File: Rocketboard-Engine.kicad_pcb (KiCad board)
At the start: 2 copper layers, 26 x 53.1 mm, 31 parts, among them IC1 STM32L072CBT6, J1 SWD Port, J2 USB_C_Receptacle_USB2.0, J3 Conn_01x20, J4 Conn_01x20, Q1 BSS138, U1 USBLC6-2SC6, U2 AMS1117-3.3

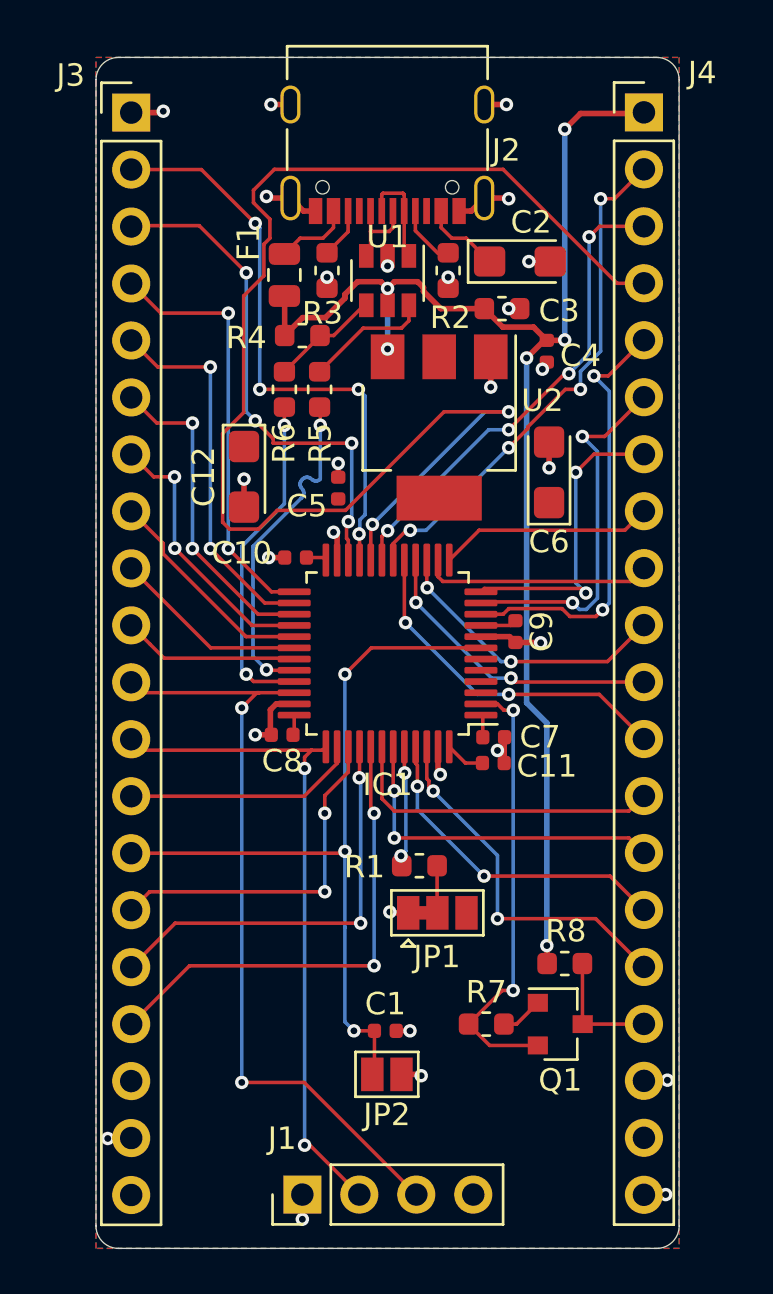
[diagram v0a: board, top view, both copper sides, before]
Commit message: Fixed unconnected copper pours/nets
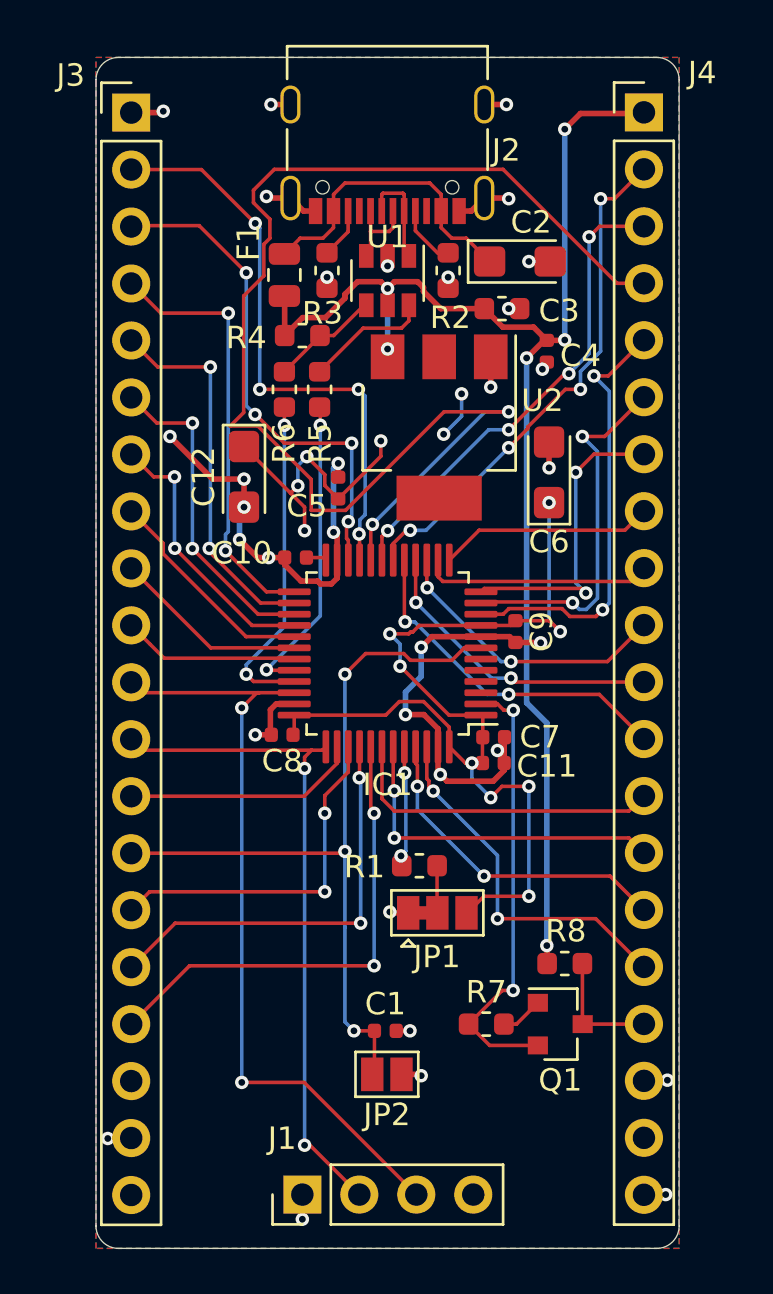
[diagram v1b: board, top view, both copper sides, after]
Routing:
- net +3V3: track 6.23 -> 61.0 mm, vias 0 -> 14
- net GND: track 33.3 -> 59.8 mm, vias 28 -> 33
- net VBUS: track 6.94 -> 13.6 mm
- net /PB2: track 60.7 -> 57.8 mm
- net /USB_D-: track 15.1 -> 14.0 mm

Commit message: Added silkscreen, fixed some placements, and generated gerbers
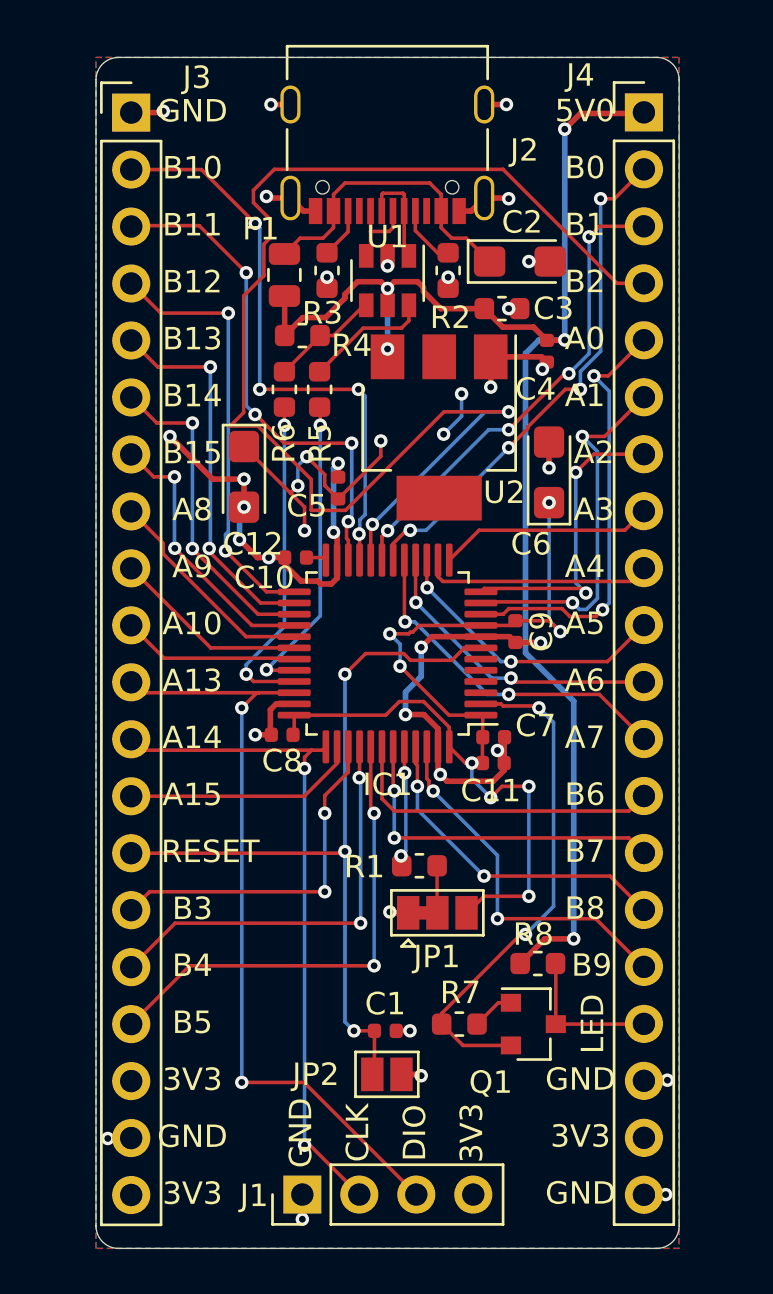
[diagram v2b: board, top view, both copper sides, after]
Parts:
- added H1: board_logo, Rocketboard-Engine:board-title, B.Cu at (134.2, 116.1)
- moved Q1 1.20 mm to (141.1, 114.9)
- moved R7 1.20 mm to (137.8, 114.9)
- moved R8 1.20 mm to (141.3, 112.2)
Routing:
- net +5V: track 62.7 -> 66.0 mm, vias 6 -> 5
- net GND: track 59.8 -> 62.4 mm
- net /LED_3v3_SIGNAL: track 20.2 -> 22.7 mm
- net /LED_5v0_SIGNAL: track 5.44 -> 6.64 mm
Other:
- board text added: "3V3"
- board text added: "5V0"
- board text added: "A0"
- board text added: "A1"
- board text added: "A10"
- board text added: "A13"
- board text added: "A14"
- board text added: "A15"
- board text added: "A2"
- board text added: "A3"
- board text added: "A4"
- board text added: "A5"
- board text added: "A6"
- board text added: "A7"
- board text added: "A8"
- board text added: "A9"
- board text added: "B0"
- board text added: "B1"
- board text added: "B10"
- board text added: "B11"
- board text added: "B12"
- board text added: "B13"
- board text added: "B14"
- board text added: "B15"
- board text added: "B2"
- board text added: "B3"
- board text added: "B4"
- board text added: "B5"
- board text added: "B6"
- board text added: "B7"
- board text added: "B8"
- board text added: "B9"
- board text added: "CLK"
- board text added: "DIO"
- board text added: "GND"
- board text added: "LED"
- board text added: "RESET"
